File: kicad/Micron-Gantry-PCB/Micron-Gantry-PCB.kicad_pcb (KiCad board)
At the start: 4 copper layers, 67 x 15 mm, 70 parts, among them J1 CAN_IN, J10 USB_C_Receptacle_USB2.0, J2 CAN_OUT, J3 M0_THERM, J4 M1_THERM, J5 Conn_01x04_Male, J6 Conn_01x04_Male, J7 ENDSTOP1, J8 ENDSTOP2, SW1 SW_Push, SW2 SW_Push, U1 TMC2209-LA-T, U2 STM32G0B1CEU6, U3 TMC2209-LA-T, U4 TCAN334, U5 NCP730BMT330TBG, Y1 Crystal_GND24

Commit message: Work in progress, layout close to finish
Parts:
- H1, H2: footprint MountingHole:MountingHole_3.2mm_M3_DIN965 -> Project:MountingHole_3.2mm_M3
- moved C18 5.40 mm to (125.8, 97.7)
- moved R12 5.40 mm to (131.2, 97.7)
- moved C11 5.40 mm to (158.8, 97.7)
- moved R6 5.40 mm to (164.2, 97.7)
- moved C29 1.50 mm to (137.5, 92.0)
- moved FB1 1.50 mm to (135.7, 92.0)
- moved U5 0.80 mm to (141.0, 92.5)
- moved C13 0.50 mm to (120.0, 87.2)
- moved C16 0.50 mm to (121.6, 87.2)
- moved C26 0.50 mm to (154.5, 98.6)
- moved C6 0.50 mm to (168.4, 96.8)
- moved SW2 0.20 mm to (155.6, 94.2)
- moved SW1 0.20 mm to (151.4, 94.2)
- moved R14 0.10 mm to (148.3, 85.5)
- moved TH1 0.10 mm to (145.0, 85.5)
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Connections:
- J3 pad 1: Net-(J3-Pad1) -> GND
- J3 pad 2: GND -> Net-(J3-Pad2)
- J4 pad 1: Net-(J4-Pad1) -> GND
- J4 pad 2: GND -> Net-(J4-Pad2)
- R11 pad 2: Net-(J4-Pad1) -> Net-(J4-Pad2)
- R12 pad 2: Net-(J4-Pad1) -> Net-(J4-Pad2)
- R5 pad 2: Net-(J3-Pad1) -> Net-(J3-Pad2)
- R6 pad 2: Net-(J3-Pad1) -> Net-(J3-Pad2)
- U2 pad 12: /ENDSTOP1 -> /CHAM_THERM
- U2 pad 13: /M0_UART -> unconnected-(U2-Pad13)
- U2 pad 14: /M0_UART_RX -> /ENDSTOP1
- U2 pad 15: unconnected-(U2-Pad15) -> /M0_UART
- U2 pad 16: unconnected-(U2-Pad16) -> /M0_UART_RX
- U2 pad 20: /M0_STEP -> /M0_DIR
- U2 pad 21: /M0_DIR -> /M0_STEP
- U2 pad 22: /M0_THERM -> unconnected-(U2-Pad22)
- U2 pad 23: /M1_THERM -> /M0_THERM
- U2 pad 24: /CHAM_THERM -> /M1_THERM
- U2 pad 44: unconnected-(U2-Pad44) -> /M1_DIAG
- U2 pad 45: /M1_STEP -> unconnected-(U2-Pad45)
- U2 pad 46: /M1_DIR -> /M1_STEP
- U2 pad 47: /M1_DIAG -> /M1_DIR
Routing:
- net +3V3: track 19.5 -> 37.8 mm, vias 6 -> 13
- net /M0_UART: track 11.9 -> 23.6 mm, vias 0 -> 2
- net /M0_DIR: track 17.5 -> 26.3 mm
- net /M1_STEP: track 36.3 -> 44.7 mm
- net /M0_DIAG: track 10.7 -> 18.8 mm
- net /M1_ENN: track 42.8 -> 50.0 mm
- net /M0_STEP: track 15.9 -> 22.7 mm
- net /ENDSTOP2: track 30.8 -> 37.5 mm
- net GND: track 67.6 -> 74.3 mm, vias 122 -> 125
- net /M1_UART: track 39.2 -> 44.3 mm, vias 1 -> 2
- net /M1_DIR: track 42.2 -> 47.2 mm
- net /M0_ENN: track 22.3 -> 26.5 mm, vias 3 -> 2
- net /CHAM_THERM: track 30.3 -> 26.4 mm, vias 1 -> 2
- net Net-(C5-Pad2): track 0.00 -> 3.89 mm
- net Net-(C13-Pad2): track 0.00 -> 3.89 mm
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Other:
- board text added: "STOP0"
- board text added: "THERM0"
- board text removed: "STOP2"
- board text removed: "THERM2"

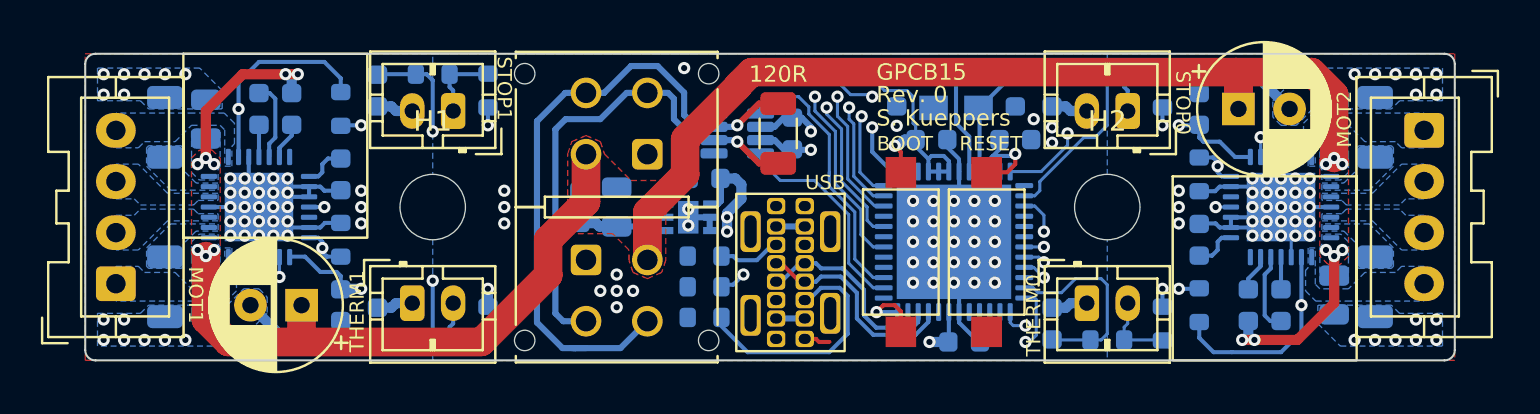
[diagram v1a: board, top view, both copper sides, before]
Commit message: Corrected USB footprint, renamed some signals
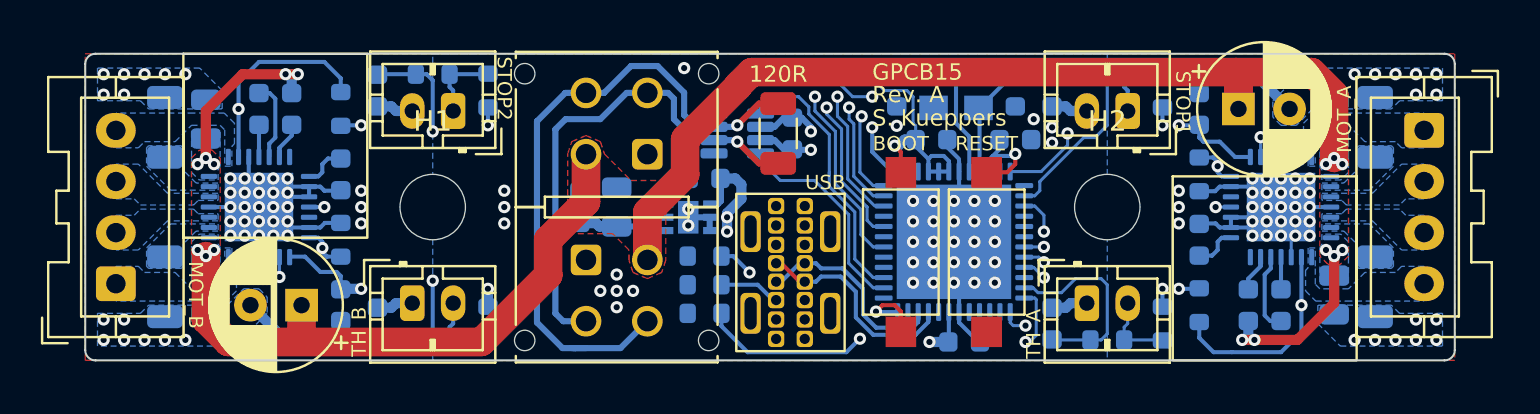
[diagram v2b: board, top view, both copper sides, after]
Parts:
- moved R15 3.00 mm to (141.8, 94.4)
- moved R13 1.40 mm to (141.8, 95.8)
- moved R16 1.30 mm to (141.8, 97.2)
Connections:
- net /M0_A1 renamed /MA_A1
- net /M0_A2 renamed /MA_A2
- net /M0_B1 renamed /MA_B1
- net /M0_B2 renamed /MA_B2
- net /M0_BRA renamed /MA_BRA
- net /M0_BRB renamed /MA_BRB
- net /M0_DIAG renamed /MA_DIAG
- net /M0_DIR renamed /MA_DIR
- net /M0_ENN renamed /MA_ENN
- net /M0_STEP renamed /MA_STEP
- net /M0_THERM renamed /MA_THERM
- net /M0_UART renamed /MA_UART
- net /M0_UART_RX renamed /MA_UART_RX
- net /M1_A1 renamed /MB_A1
- net /M1_A2 renamed /MB_A2
- net /M1_B1 renamed /MB_B1
- net /M1_B2 renamed /MB_B2
- net /M1_BRA renamed /MB_BRA
- net /M1_BRB renamed /MB_BRB
- net /M1_DIAG renamed /MB_DIAG
- net /M1_DIR renamed /MB_DIR
- net /M1_ENN renamed /MB_ENN
- net /M1_STEP renamed /MB_STEP
- net /M1_THERM renamed /MB_THERM
- net /M1_UART renamed /MB_UART
- net /M1_UART_RX renamed /MB_UART_RX
- J10 pad A5: /USB_CC1 -> Net-(R15-Pad1)
- J10 pad A8: Net-(J10-PadA8) -> unconnected-(J10-PadA8)
- J10 pad B5: /USB_CC2 -> Net-(R13-Pad1)
- J10 pad B8: Net-(J10-PadB8) -> unconnected-(J10-PadB8)
- R13 pad 1: Net-(J10-PadB8) -> Net-(R13-Pad1)
- R15 pad 1: Net-(J10-PadA8) -> Net-(R15-Pad1)
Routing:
- net Net-(R15-Pad1): track 0.00 -> 17.0 mm, vias 0 -> 1
- net Net-(J10-PadA8): track 11.4 -> 0.00 mm
- net GND: track 74.3 -> 82.4 mm
- net Net-(J10-PadA4): track 2.80 -> 7.40 mm
- net /BOOT0: track 16.3 -> 13.2 mm
- net Net-(J10-PadB8): track 3.07 -> 0.00 mm
- net Net-(R13-Pad1): track 0.00 -> 2.99 mm
- added copper zone on In2.Cu, net +3V3
- removed copper zone on In1.Cu, net +3V3
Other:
- board text added: "MOT_A"
- board text added: "MOT_B"
- board text added: "Rev. A"
- board text added: "STOP2"
- board text added: "TH_A"
- board text added: "TH_B"
- board text removed: "MOT1"
- board text removed: "MOT2"
- board text removed: "Rev. 0"
- board text removed: "STOP0"
- board text removed: "THERM0"
- board text removed: "THERM1"
